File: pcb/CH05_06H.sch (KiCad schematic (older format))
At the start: 8 parts

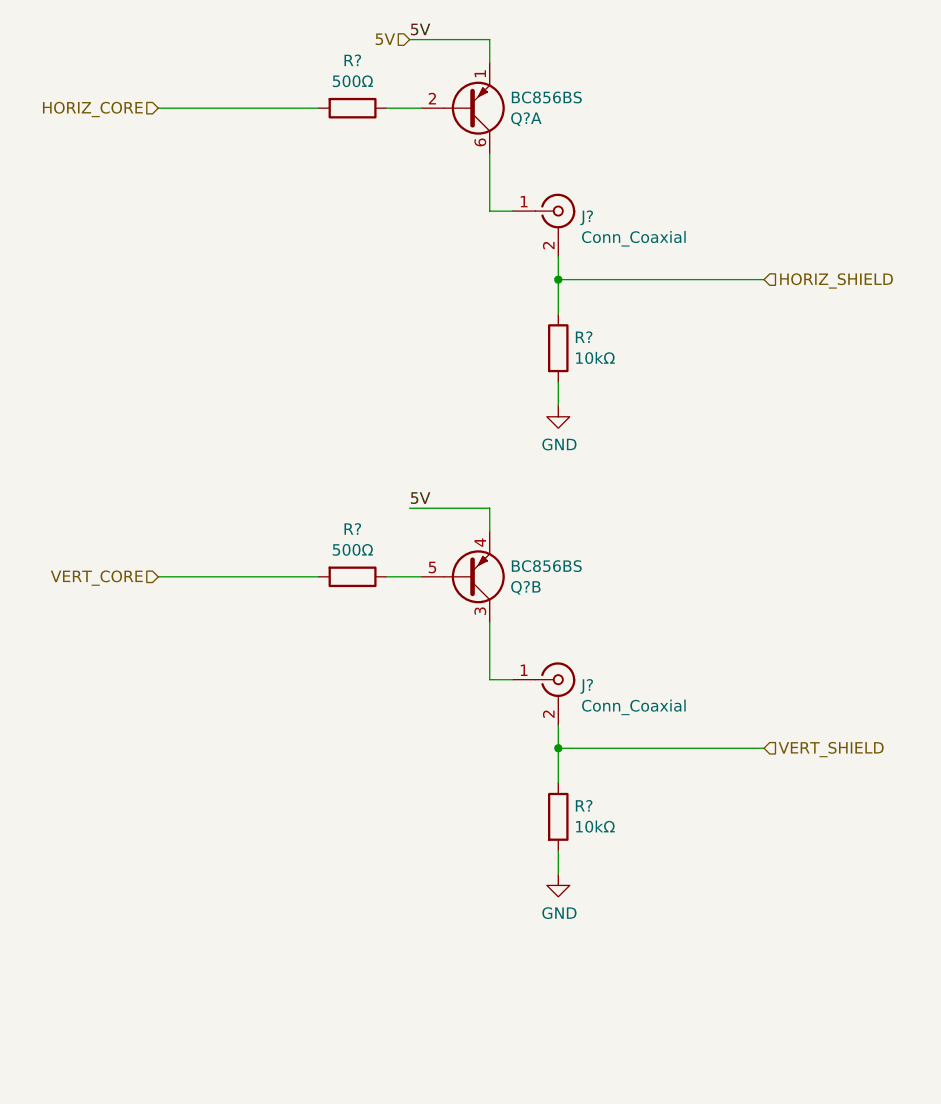
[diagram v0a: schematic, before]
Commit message: Completes first cut of the schematic
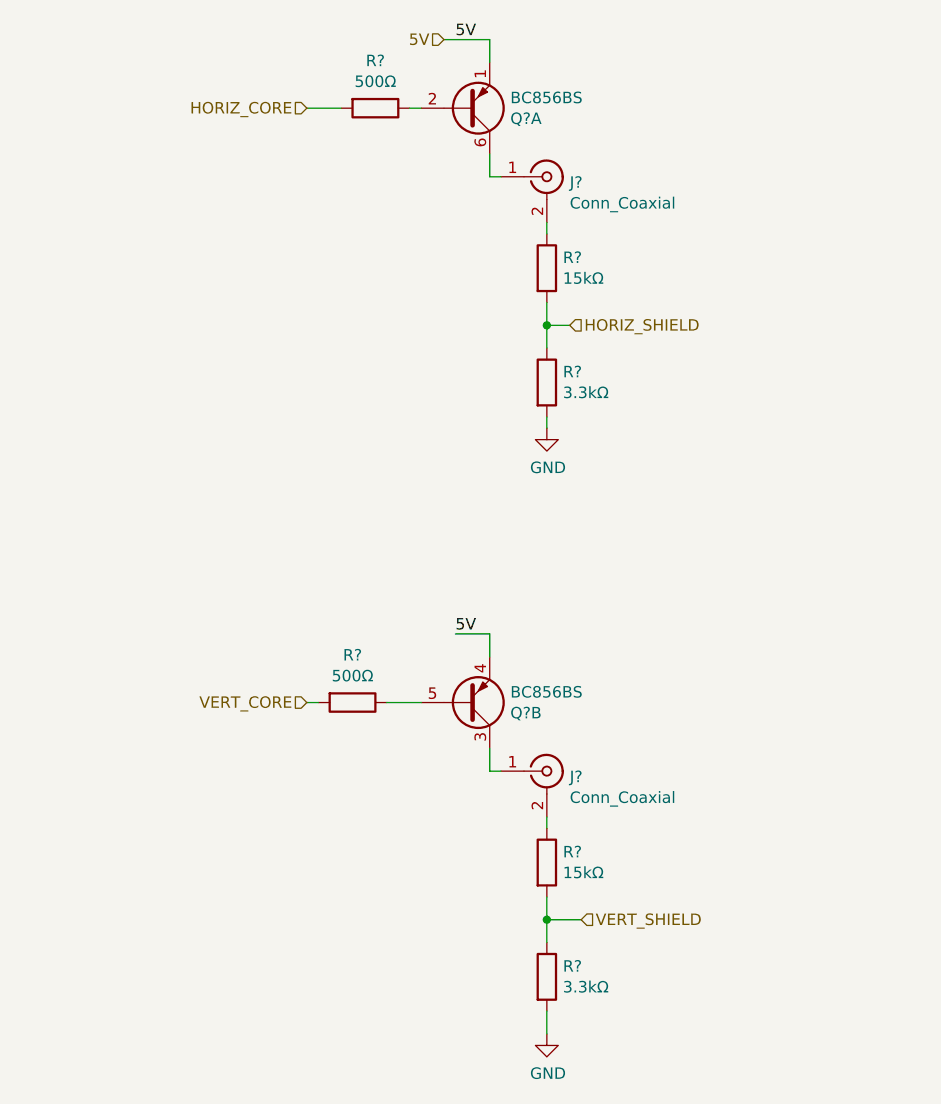
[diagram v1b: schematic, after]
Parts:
- removed R? (x2): 10kΩ, Resistor_SMD:R_0805_2012Metric, symbol Device:R
- added R? (x2): 15kΩ, Resistor_SMD:R_0805_2012Metric, symbol Device:R
- added R? (x2): 3.3kΩ, Resistor_SMD:R_0805_2012Metric, symbol Device:R
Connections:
- net GND: now also R?.2, R?.2
- net HORIZ_SHIELD: now also R?.1, R?.2; no longer J?.2 (Ext)
- net VERT_SHIELD: now also R?.1, R?.2; no longer J?.2 (Ext)
- new net: J?.2 (Ext), R?.1 (x2)
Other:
- moved on the sheet: J?, Q?B, R?

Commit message: Updates schematic based on some testing. Adds PDF for review
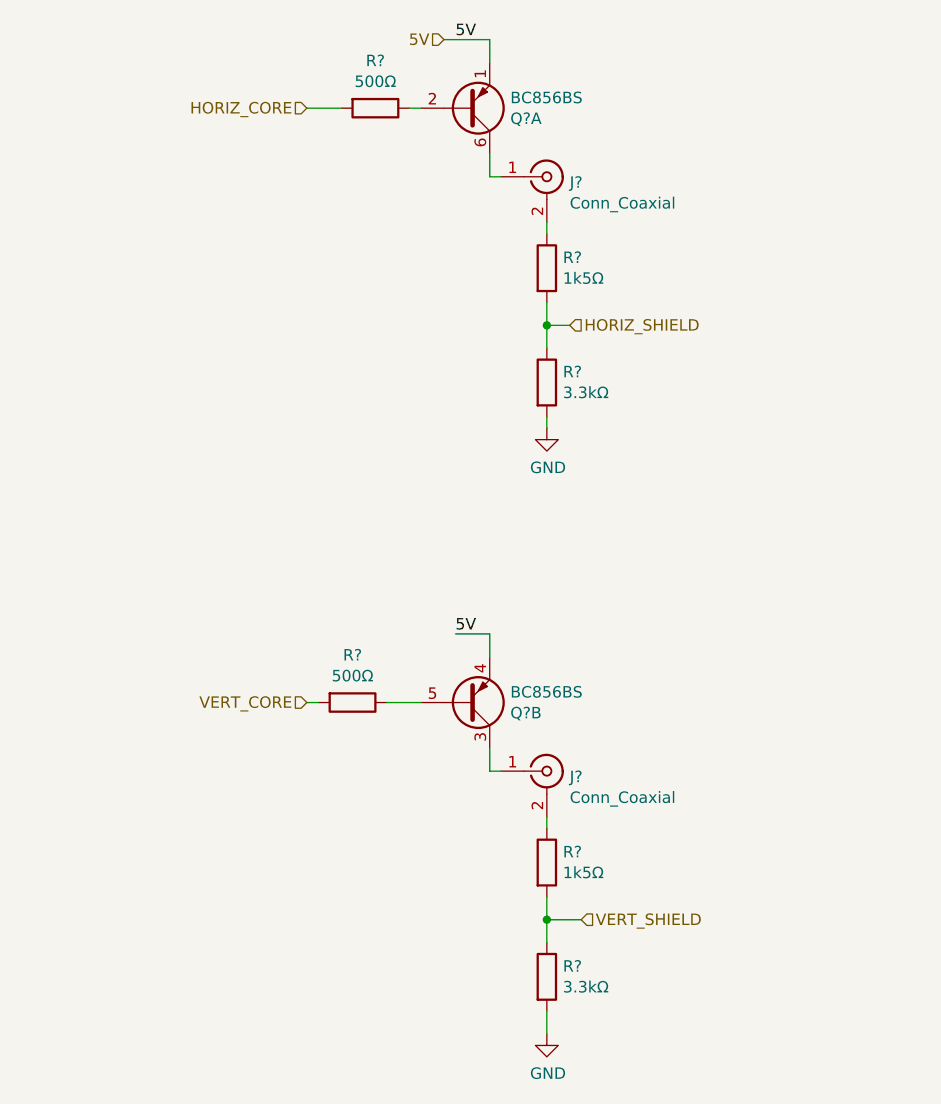
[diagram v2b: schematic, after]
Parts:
- R? (x2): value 15kΩ -> 1k5Ω
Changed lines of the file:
@@
 AR Path="/61C60B45/61C64A50/61B757DD" Ref="R?"  Part="1"
 F 0 "R?" H 4620 2796 50  0000 L CNN
-F 1 "15kΩ" H 4620 2705 50  0000 L CNN
+F 1 "1k5Ω" H 4620 2705 50  0000 L CNN
 F 2 "Resistor_SMD:R_0805_2012Metric" V 4480 2750 50  0001 C CNN
 F 3 "~" H 4550 2750 50  0001 C CNN
@@
 AR Path="/61C60B45/61C64A50/61B7E30B" Ref="R?"  Part="1"
 F 0 "R?" H 4620 5396 50  0000 L CNN
-F 1 "15kΩ" H 4620 5305 50  0000 L CNN
+F 1 "1k5Ω" H 4620 5305 50  0000 L CNN
 F 2 "Resistor_SMD:R_0805_2012Metric" V 4480 5350 50  0001 C CNN
 F 3 "~" H 4550 5350 50  0001 C CNN
